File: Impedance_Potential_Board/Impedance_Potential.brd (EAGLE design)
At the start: 70 x 70 mm, 85 parts, among them IC1 MAX30001GCWV+, J1 Header, U4 AP2112K-1.8V

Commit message: Board Updates
Separated analog and digital ground
Updated routing
Updated silk labeling
Sound board with ES8388 included
Impedance and ECG board
Working on IMU board
Working on Environmental Airquality board
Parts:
- added U$1: (no value), SparkFun-Aesthetics:OSHW-LOGO-M
- moved C14 0.50 mm to (30.6, 48.8)
- moved C15 0.50 mm to (45.0, 46.7)
- moved C13 0.45 mm to (30.6, 47.2)
- moved U4 0.20 mm to (47.8, 46.5)
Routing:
- net GND: vias 51 -> 56
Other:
- board text added: "Utzinger"
- board text added: "V2 2024"

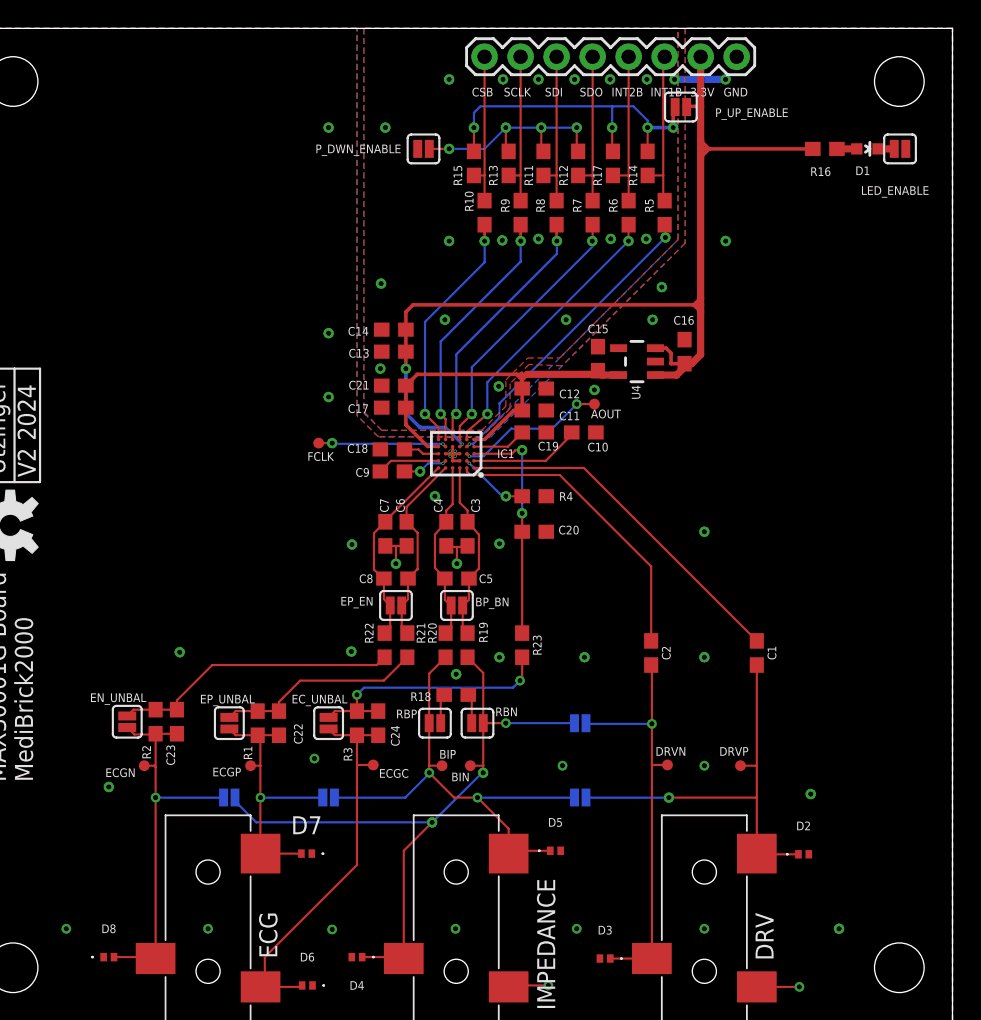
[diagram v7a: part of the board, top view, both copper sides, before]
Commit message: IMU board
Completed IMU board design
Updated designs with ground via close to any other via.
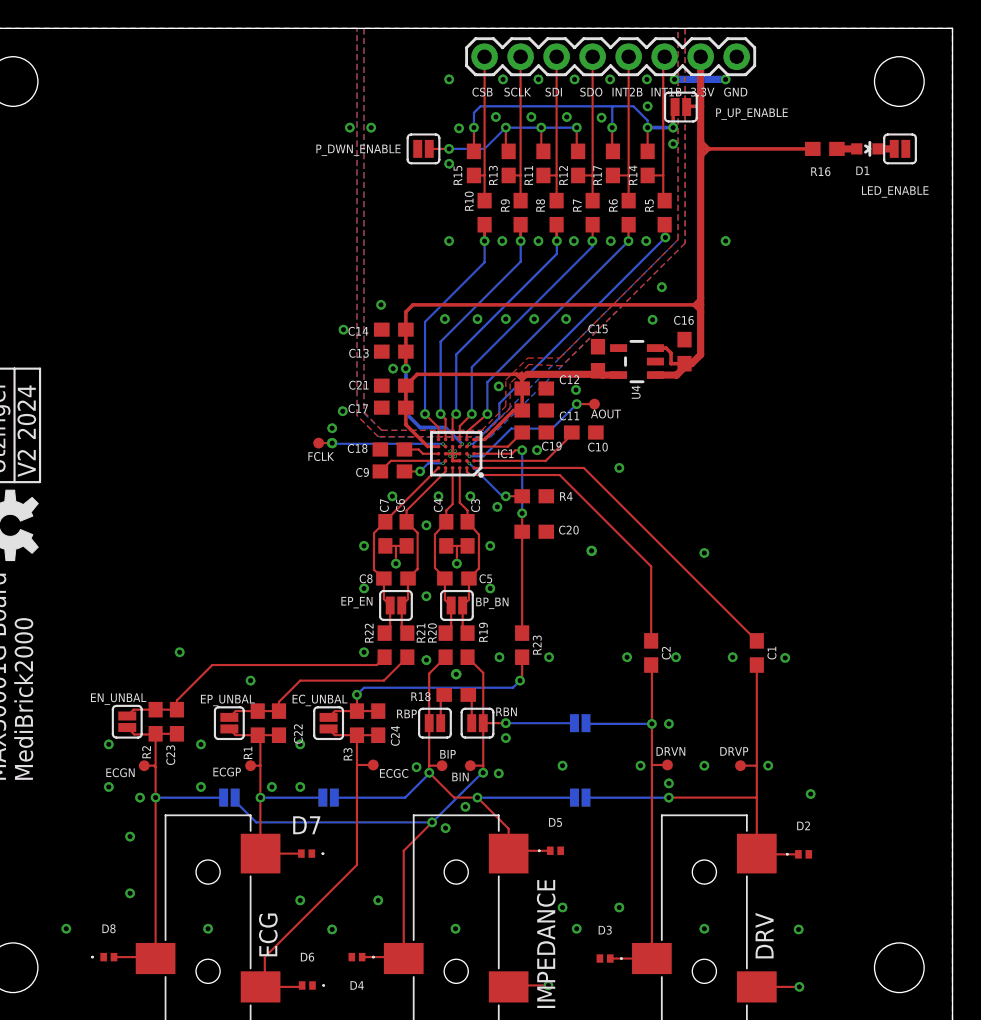
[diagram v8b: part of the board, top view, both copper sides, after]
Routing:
- net GND: track 18.6 -> 18.7 mm, vias 56 -> 105
